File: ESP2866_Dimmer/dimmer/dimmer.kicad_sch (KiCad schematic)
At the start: 40 parts, among them J1 Conn_01x04_Male, J2 Screw_Terminal_01x04, J3 Conn_01x03_Male, J4 Conn_01x03_Male, J5 Screw_Terminal_01x02, J6 Screw_Terminal_01x02, J7 Screw_Terminal_01x02, K1 TIANBO-HJR-4102-L, Q1 2N3904, SW1 SW_Push, U1 B1203S-1WR3, U2 LTV-354T, U3 ESP-12E, U4 L78L05_SOT89, U5 LTV-354T, U6 LTV-354T, U7 LTV-354T, U8 LTV-354T

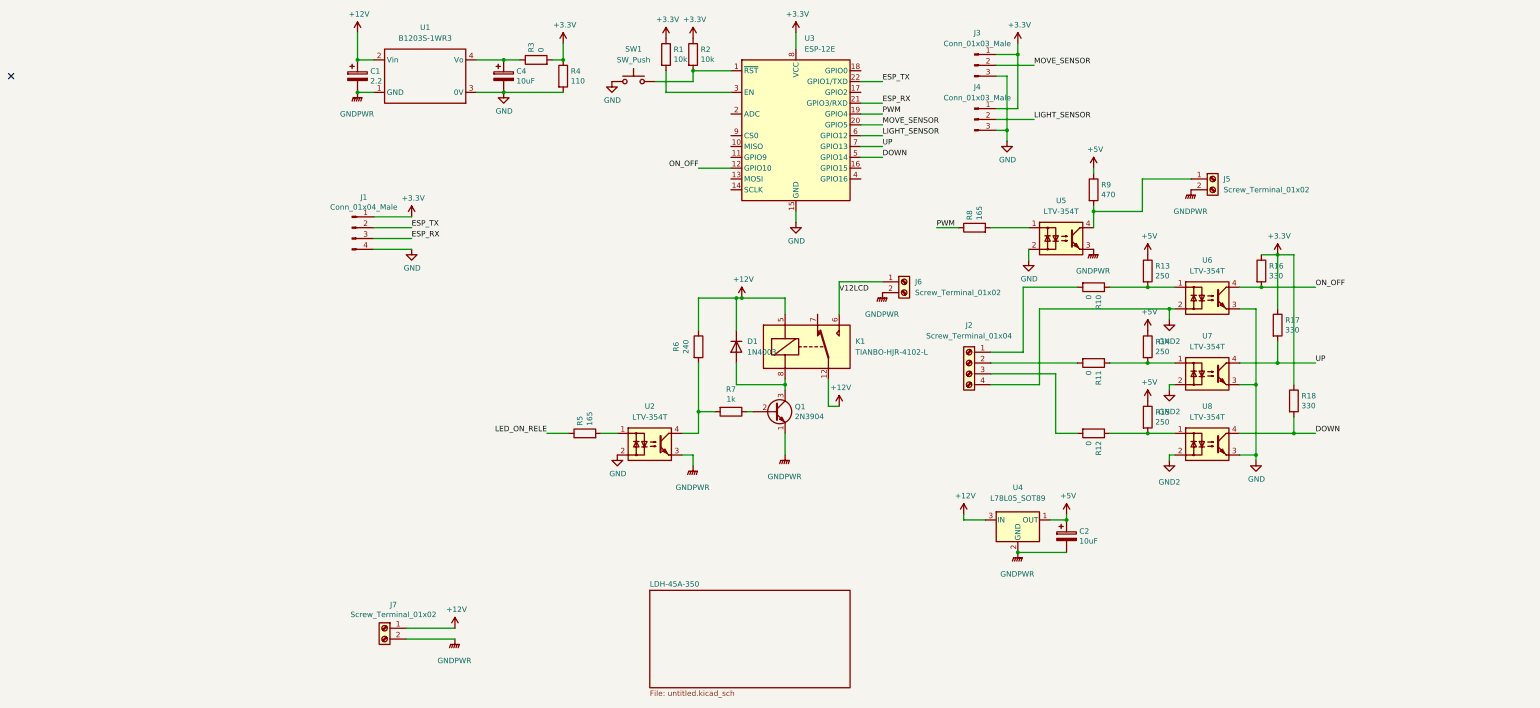
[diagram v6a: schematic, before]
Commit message: Окремий проект для плати драйверу.
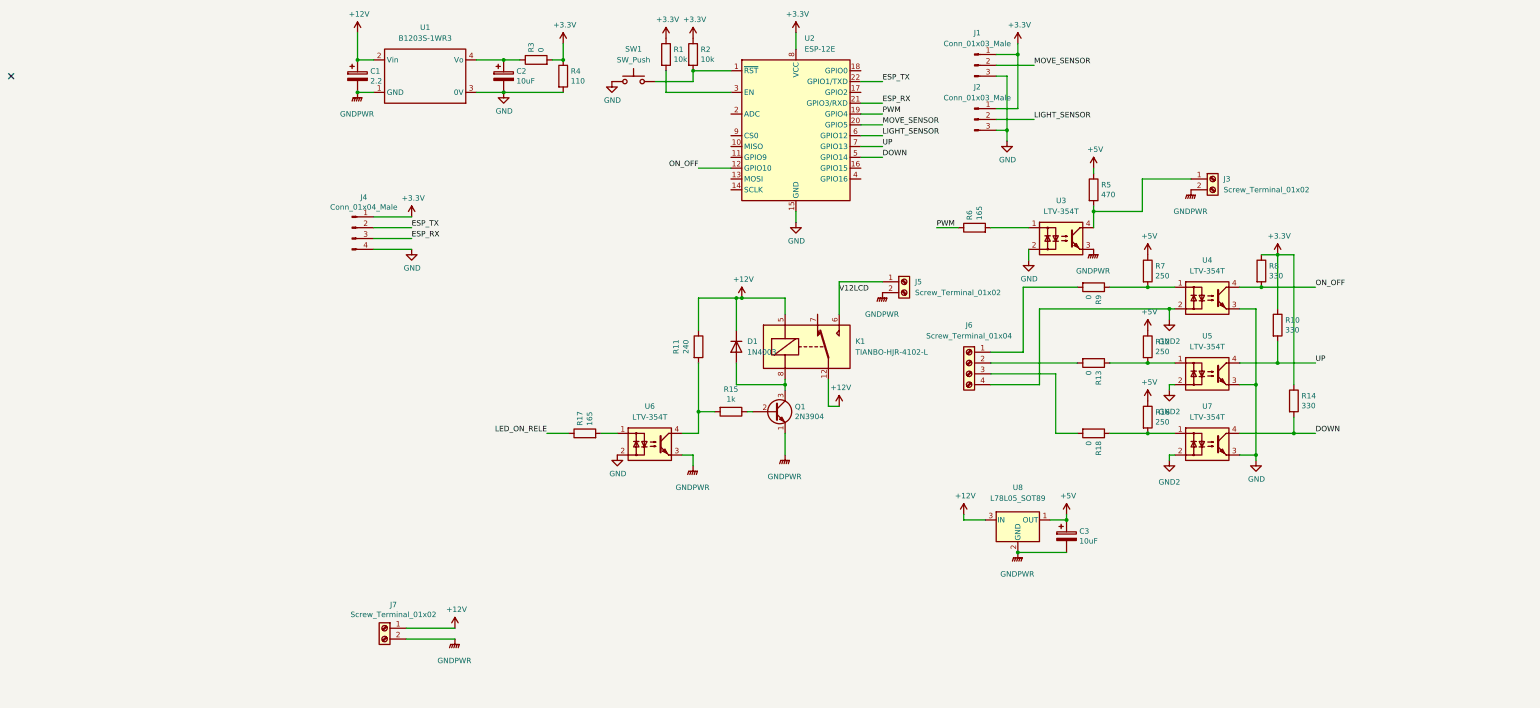
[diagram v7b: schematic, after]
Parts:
- renumbered C4 to C2, C2 to C3, J3 to J1, J4 to J2, J5 to J3, J1 to J4, J6 to J5, J2 to J6, R17 to R10, R6 to R11, R14 to R12, R11 to R13, R18 to R14, R7 to R15, R15 to R16, R5 to R17, R12 to R18, R9 to R5, R8 to R6, R13 to R7, R16 to R8, R10 to R9, U3 to U2, U5 to U3, U6 to U4, U7 to U5, U2 to U6, U8 to U7, U4 to U8
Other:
- removed sheet LDH-45A-350

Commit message: Upd
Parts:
- removed J3, J5: Screw_Terminal_01x02, Connector_JST:JST_NV_B02P-NV_1x02_P5.00mm_Vertical, symbol Connector:Screw_Terminal_01x02
- added F1: Fuse, Fuse:Fuse_2920_7451Metric_Pad2.10x5.45mm_HandSolder, symbol Device:Fuse
- added J2: Screw_Terminal_01x02, TerminalBlock_MetzConnect:TerminalBlock_MetzConnect_Type011_RT05502HBWC_1x02_P5.00mm_Horizontal, symbol Connector:Screw_Terminal_01x02
- added R5, R6: 0, Resistor_SMD:R_1206_3216Metric_Pad1.30x1.75mm_HandSolder, symbol Device:R
- added U1: LDH-45A-350, dimmer:LDH-45A, symbol dimmer_lib:LDH-45A-350
- J3: renamed from J2; footprint (none) -> Connector_JST:JST_EH_B3B-EH-A_1x03_P2.50mm_Vertical
- SW1: footprint Button_Switch_SMD:SW_DIP_SPSTx01_Slide_6.7x4.1mm_W6.73mm_P2.54mm_LowProfile_JPin -> Button_Switch_THT:SW_PUSH_6mm
- U2: renamed from U1; footprint (none) -> dimmer:B1203-1WR3
- renumbered J6 to J5, J7 to J6, R8 to R10, R9 to R11, R10 to R12, R11 to R13, R12 to R14, R13 to R15, R14 to R16, R15 to R17, R16 to R18, R17 to R19, R18 to R20, R5 to R7, R6 to R8, R7 to R9, U2 to U3, U3 to U4, U4 to U5, U5 to U6, U6 to U7, U7 to U8, U8 to U9
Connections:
- net +5V: now also R6.2
- net GNDPWR: now also R5.1, U1.2 (Vin-), U1.3 (DIM-)
- net V12LCD: now also F1.2, U1.1 (Vin+); no longer K1.6
- net at R7.2, U4.4: now also U1.5 (PWM_DIM)
- new net: F1.1, K1.6
- new net: R5.2, R6.1, U1.4 (Analog_DIM)
- new net: J2.2 (Pin_2), U1.6 (Vout-)
- new net: J2.1 (Pin_1), U1.7 (Vout+)
